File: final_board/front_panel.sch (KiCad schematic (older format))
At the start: 10 parts, among them P100 ISP, P101 DEBUG_LED

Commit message: Final changes to board
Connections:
- net +5V renamed +12V
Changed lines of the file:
@@
 EESchema Schematic File Version 2
-LIBS:final_outline-rescue
 LIBS:power
 LIBS:device
@@
 LIBS:MITEVT_power
 LIBS:MITEVT_REG
+LIBS:zsr1000gta
 LIBS:final_outline-cache
 EELAYER 25 0
@@
 $EndComp
 Text HLabel 2800 2050 0    60   Output ~ 0
-+5V
++12V
 Text HLabel 4300 2050 2    60   Output ~ 0
 RXD
@@
 MCU_PROG_N
 $Comp
-L GND #PWR06
+L GND #PWR07
 U 1 1 563E4869
 P 5300 1900
-F 0 "#PWR06" H 5300 1650 50  0001 C CNN
+F 0 "#PWR07" H 5300 1650 50  0001 C CNN
 F 1 "GND" H 5300 1750 50  0000 C CNN
 F 2 "" H 5300 1900 60  0000 C CNN
@@
 LED1
 $Comp
-L GND #PWR07
+L GND #PWR08
 U 1 1 563E4469
 P 2200 3200
-F 0 "#PWR07" H 2200 2950 50  0001 C CNN
+F 0 "#PWR08" H 2200 2950 50  0001 C CNN
 F 1 "GND" H 2200 3050 50  0000 C CNN
 F 2 "" H 2200 3200 60  0000 C CNN

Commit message: Fixed some routing
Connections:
- net +12V renamed +5V
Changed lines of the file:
@@
 LIBS:MITEVT_power
 LIBS:MITEVT_REG
-LIBS:zsr1000gta
 LIBS:final_outline-cache
 EELAYER 25 0
@@
 $EndComp
 Text HLabel 2800 2050 0    60   Output ~ 0
-+12V
++5V
 Text HLabel 4300 2050 2    60   Output ~ 0
 RXD

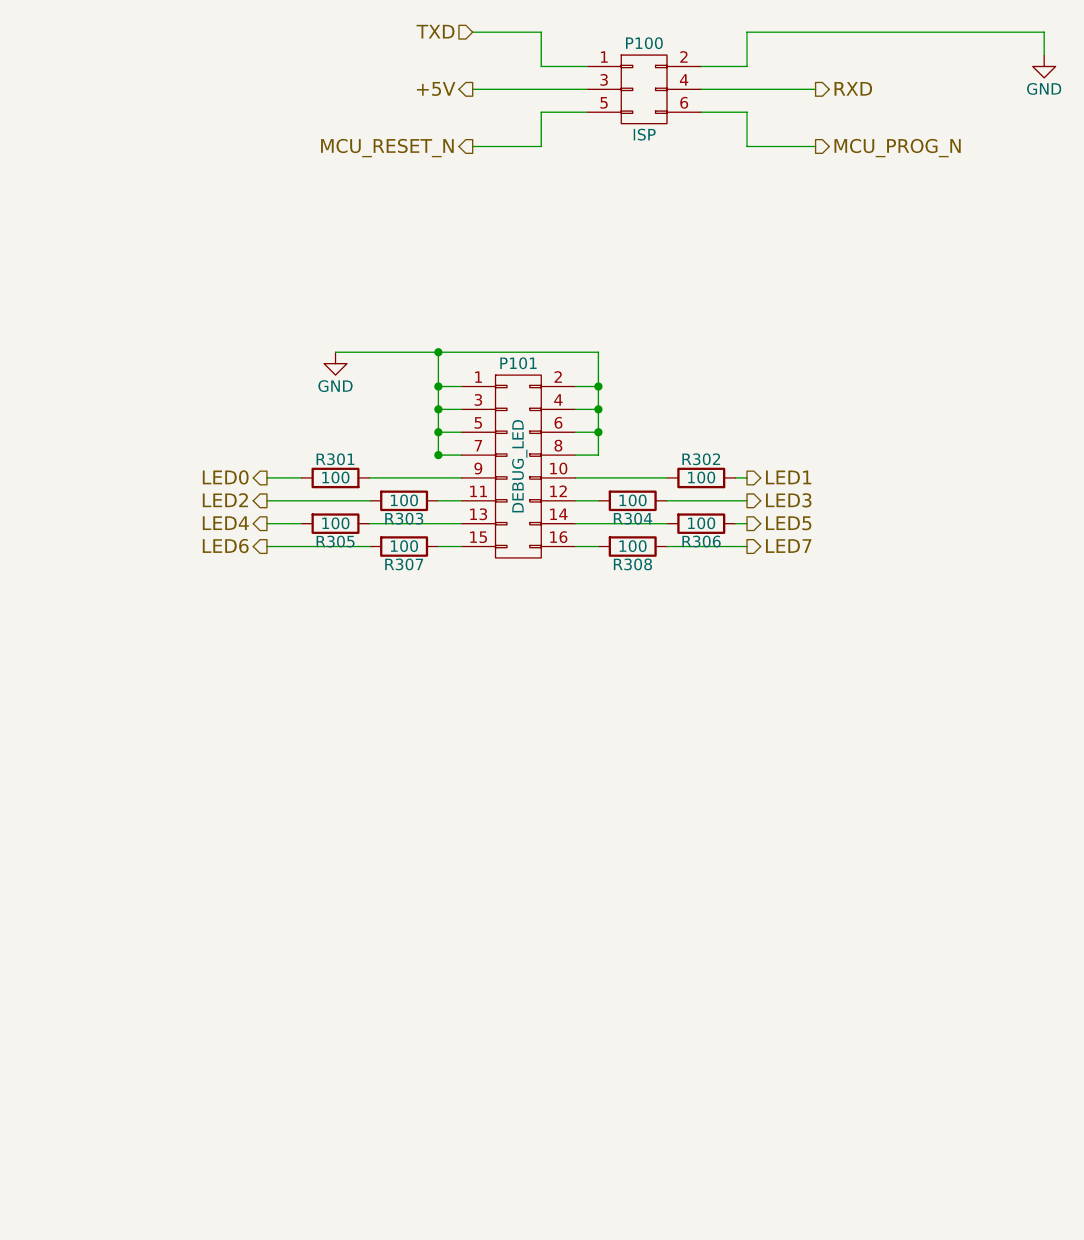
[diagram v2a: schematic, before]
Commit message: Updated PCB by replacing old parts, fixing voltage regulator, adding test points, and general improvements
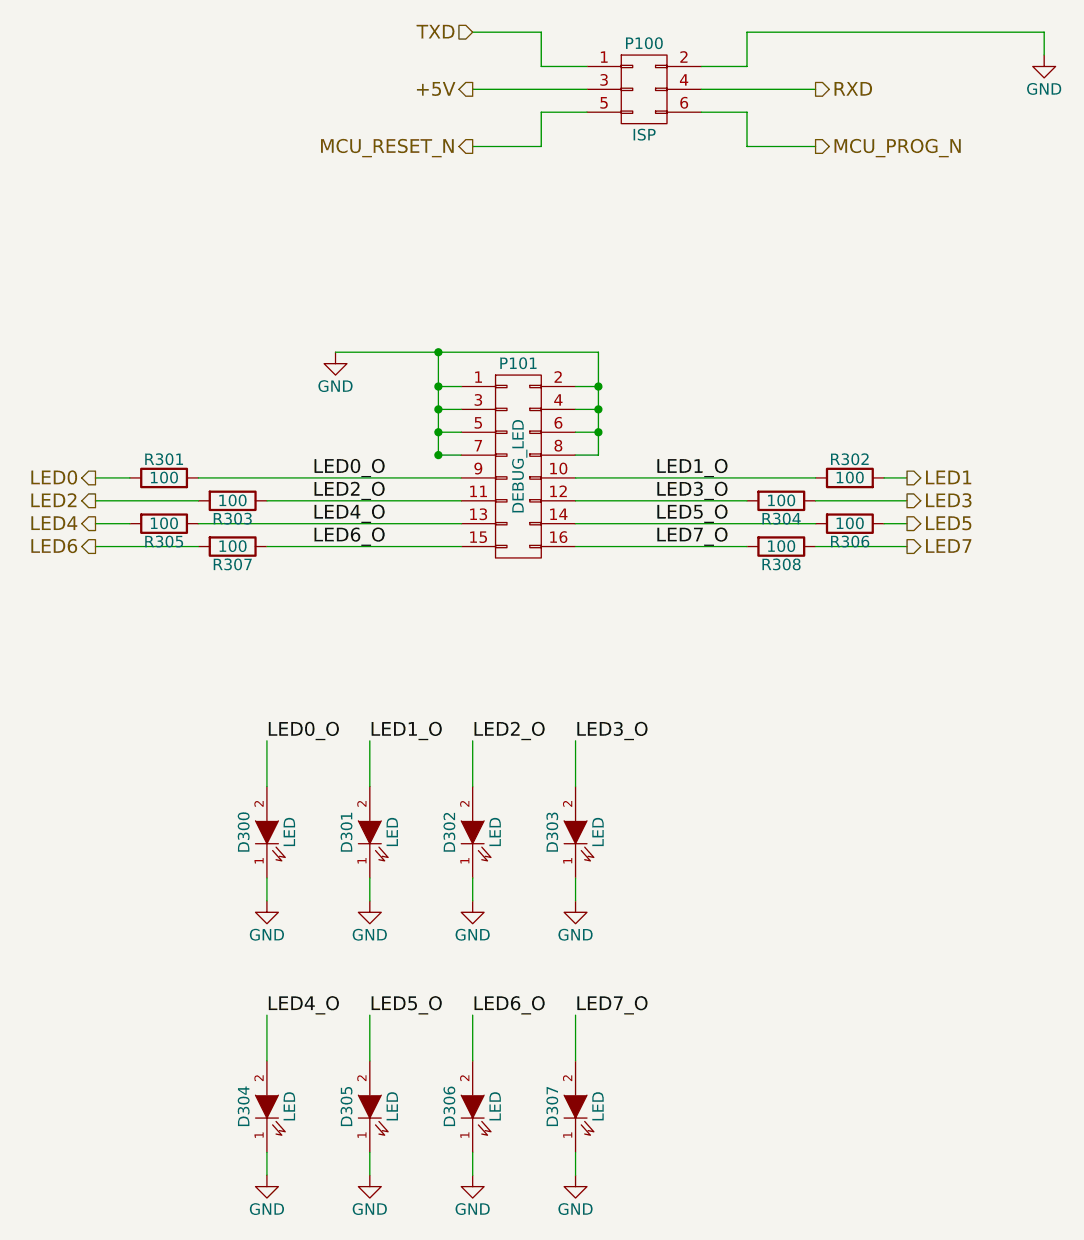
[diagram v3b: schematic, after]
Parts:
- added D300, D301, D302, D303, D304, D305, D306, D307: LED, LEDs:LED_0805, symbol LED
- P100: footprint Pin_Headers:Pin_Header_Straight_2x03 -> Connectors_Molex:Molex_Microfit3_Header_02x03_Angled_43045-060x
- P101: footprint LEDs:LED-0805 -> Connectors_Molex:Molex_Microfit3_Header_02x08_Angled_43045-160x
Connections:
- net GND: now also D300.1 (K), D301.1 (K), D302.1 (K), D303.1 (K), D304.1 (K), D305.1 (K), D306.1 (K), D307.1 (K)
- net LED1_O: now reaches P101.10 (P10), R302.1
- net LED1_O: now also D301.2 (A)
- net LED2_O: now reaches P101.11 (P11), R303.1
- net LED2_O: now also D302.2 (A)
- net LED3_O: now reaches P101.12 (P12), R304.2
- net LED3_O: now also D303.2 (A)
- net LED4_O: now reaches P101.13 (P13), R305.1
- net LED4_O: now also D304.2 (A)
- net LED5_O: now reaches P101.14 (P14), R306.2
- net LED5_O: now also D305.2 (A)
- net LED6_O: now reaches P101.15 (P15), R307.1
- net LED6_O: now also D306.2 (A)
- net LED7_O: now reaches P101.16 (P16), R308.2
- net LED7_O: now also D307.2 (A)
- net LED0_O: now reaches P101.9 (P9), R301.2
- net LED0_O: now also D300.2 (A)
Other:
- moved on the sheet: R301, R302, R303, R304, R305, R306, R307, R308
